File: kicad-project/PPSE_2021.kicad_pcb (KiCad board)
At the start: 2 copper layers, 100 x 60 mm, 133 parts, among them J1 Conn_02x03_Counter_Clockwise, J10 Motor 2, J11 Panel+ Connector, J2 Conn_02x08_Counter_Clockwise, J3 USB_B_Mini, J4 12V IN, J5 Compass, J6 Accelerometer, J7 OLED, J8 Panel- Connector, J9 Motor 1, Q1 3LP01M, Q10 SI2300DS, Q11 SI2300DS, Q12 SI2300DS, Q13 SI2300DS, Q2 PDTC114Y, Q3 BC846A, Q4 BC846A, Q5 BC846A, Q6 SI2300DS, Q7 SI2300DS, Q8 SI2300DS, Q9 SI2300DS, SW1 PRG_SW, SW2 RST_SW, SW3 HOME_SW, SW4 EN_SW, U1 W25Q16JVSS, U2 RP2040, U3 TPS563201, U4 PAM-7Q-0, Y1 12MHz

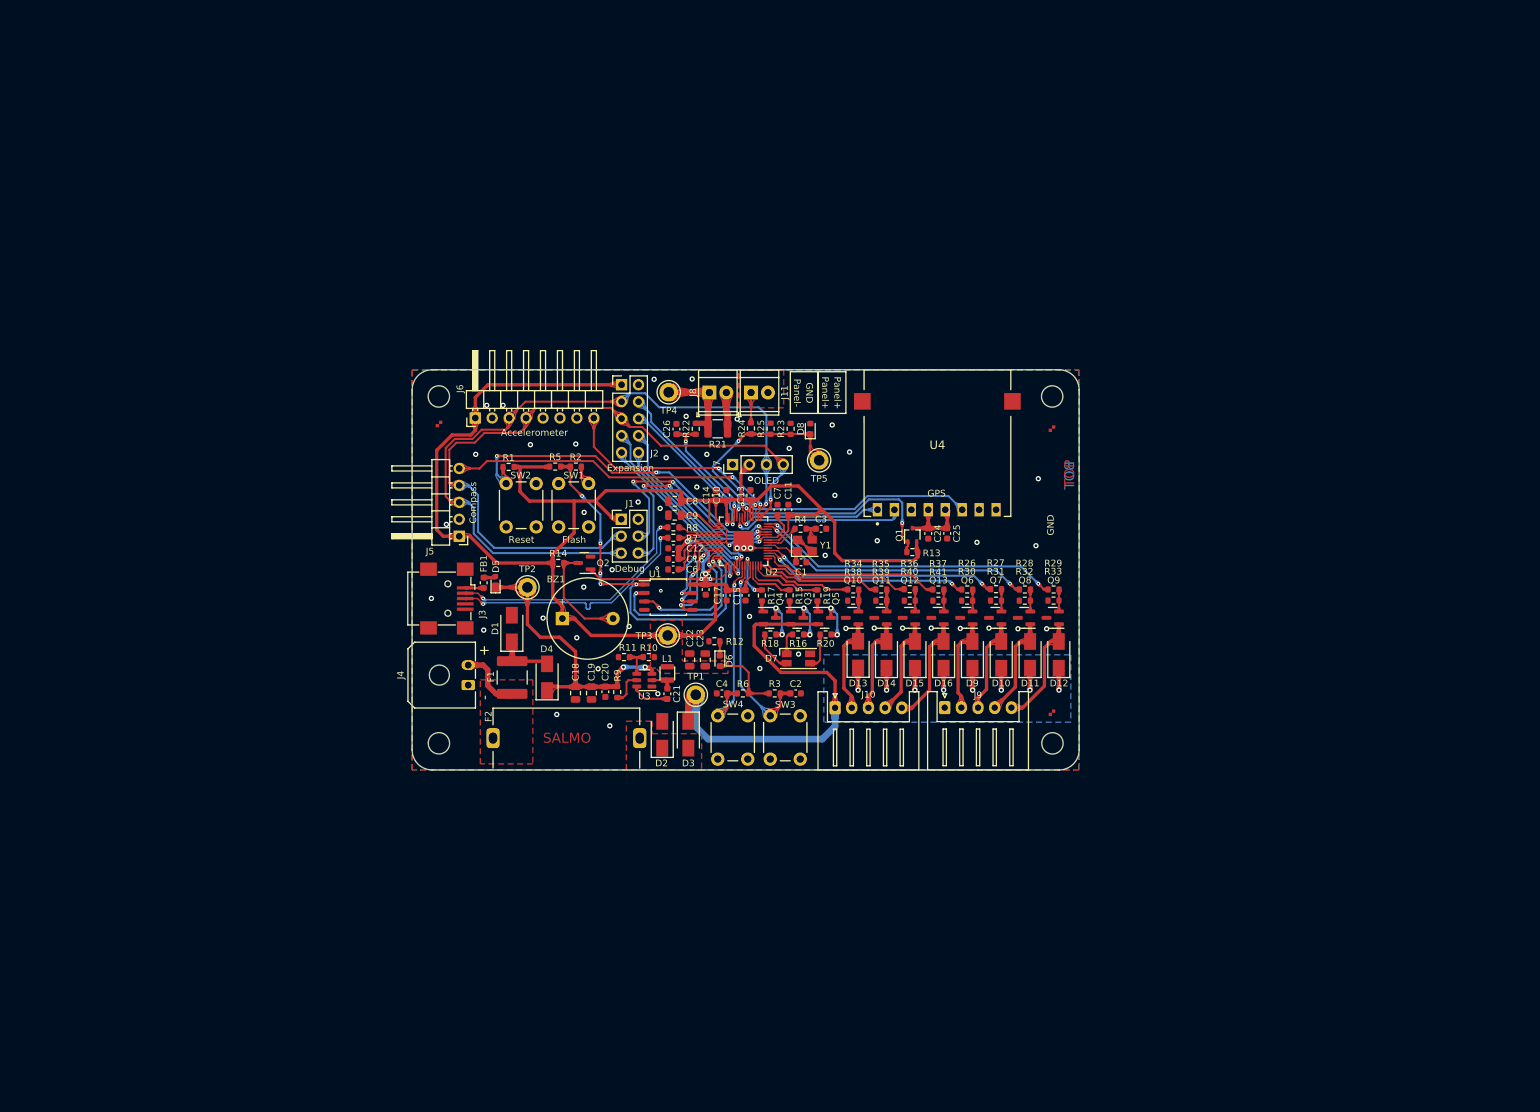
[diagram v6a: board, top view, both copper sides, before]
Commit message: report: add screenshots of steps of layout
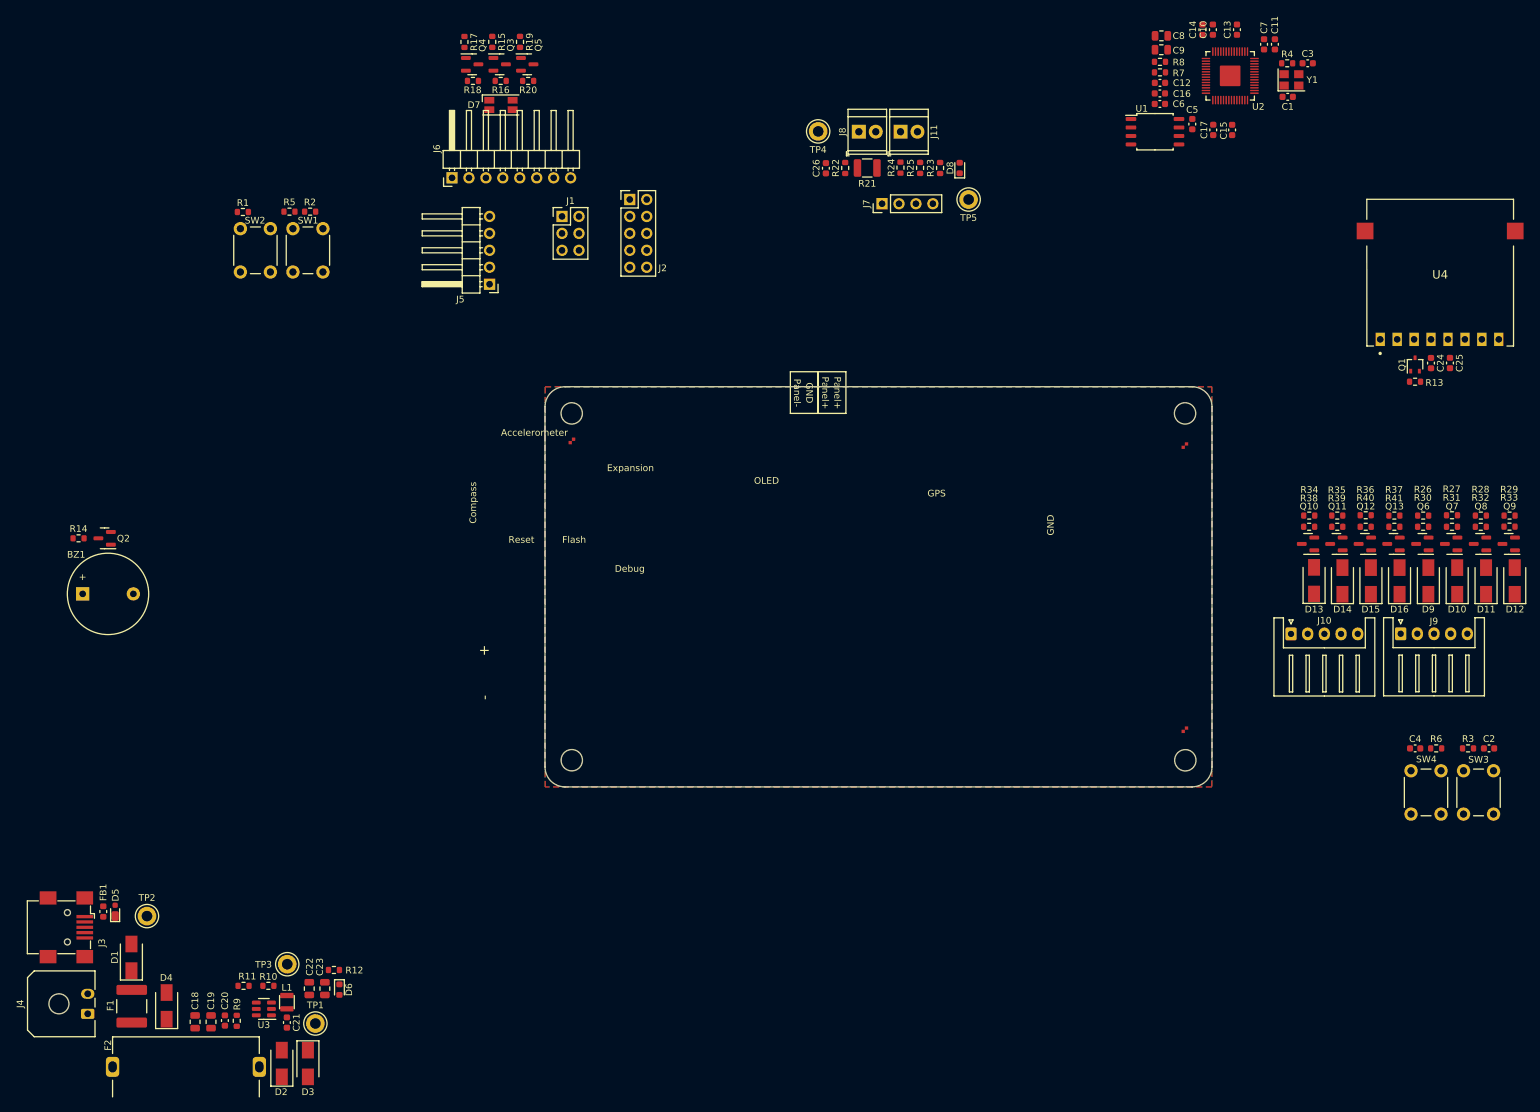
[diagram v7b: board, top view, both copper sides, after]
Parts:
- moved C2 104.3 mm to (249.0, 131.7)
- moved C4 104.3 mm to (237.9, 131.7)
- moved R6 104.3 mm to (241.1, 131.7)
- moved SW4 104.3 mm to (237.3, 141.5)
- moved R3 104.3 mm to (245.8, 131.7)
- moved SW3 104.3 mm to (245.2, 141.5)
- moved C1 101.0 mm to (218.8, 34.0)
- moved C12 101.0 mm to (199.6, 31.9)
- moved C13 101.0 mm to (211.2, 23.9)
- moved C14 101.0 mm to (206.0, 23.9)
- moved C16 101.0 mm to (199.6, 33.5)
- moved C3 101.0 mm to (221.8, 29.0)
- moved C5 101.0 mm to (204.5, 38.1)
- moved C6 101.0 mm to (199.6, 35.1)
- moved C7 101.0 mm to (215.2, 26.1)
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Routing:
- net +3V3: track 286.5 -> 0.00 mm, vias 2 -> 0
- net /Connectivity/SCL: track 108.7 -> 0.00 mm, vias 1 -> 0
- net /Connectivity/SDA: track 104.8 -> 0.00 mm, vias 1 -> 0
- net +12V: track 91.9 -> 0.00 mm, vias 8 -> 0
- net /Control/~{FLASH_CS}: track 55.6 -> 0.00 mm, vias 6 -> 0
- net /Control/~{RESET}: track 53.4 -> 0.00 mm, vias 3 -> 0
- net /Connectivity/DRDY: track 50.6 -> 0.00 mm, vias 2 -> 0
- net /Actuation/M1_W22: track 46.1 -> 0.00 mm, vias 2 -> 0
- net /Power/SW_VIN: track 43.5 -> 0.00 mm, vias 2 -> 0
- net /Actuation/M1_W21: track 41.6 -> 0.00 mm, vias 2 -> 0
- net /Control/USB_D+: track 37.7 -> 0.00 mm, vias 2 -> 0
- net /Control/USB_D-: track 37.2 -> 0.00 mm, vias 2 -> 0
- net /Connectivity/GPS_TP: track 37.0 -> 0.00 mm, vias 1 -> 0
- net /Actuation/M1_W12: track 35.8 -> 0.00 mm, vias 2 -> 0
- net /Control/SWCLK: track 34.9 -> 0.00 mm, vias 3 -> 0
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- removed copper zone on B.Cu, net +12V
- removed copper zone on F.Cu, net +3V3
- removed copper zone on F.Cu, net /Power/12V_IN
- removed copper zone on F.Cu, net /Power/12V_Post_Fuse
- removed copper zone on F.Cu, net /Sensing/Panel+
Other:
- board text removed: "BOT"
- board text removed: "SALMO"
- board text removed: "TOP"
